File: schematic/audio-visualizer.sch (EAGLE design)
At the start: 18 parts, among them J3 455-1750-1-ND, U1 MSGEQ7P, U2 SN74AHCT125N

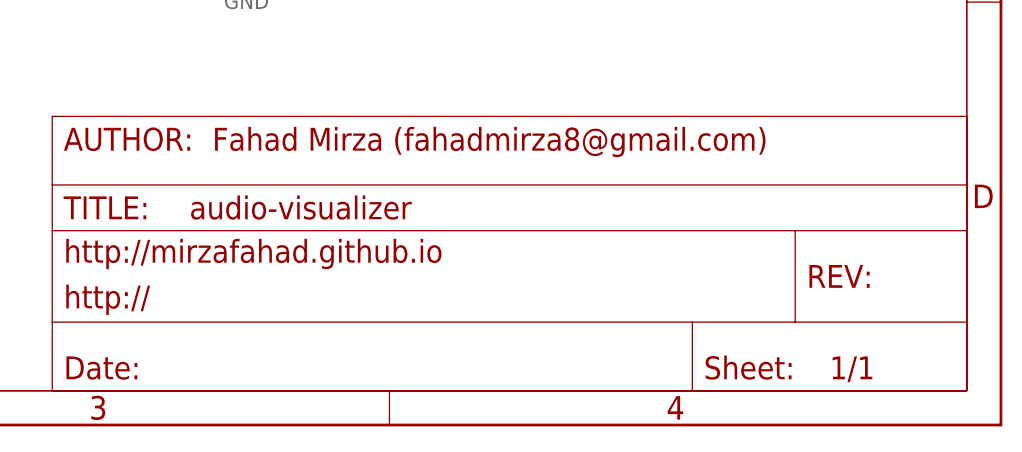
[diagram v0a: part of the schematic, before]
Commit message: pdf schematic added.
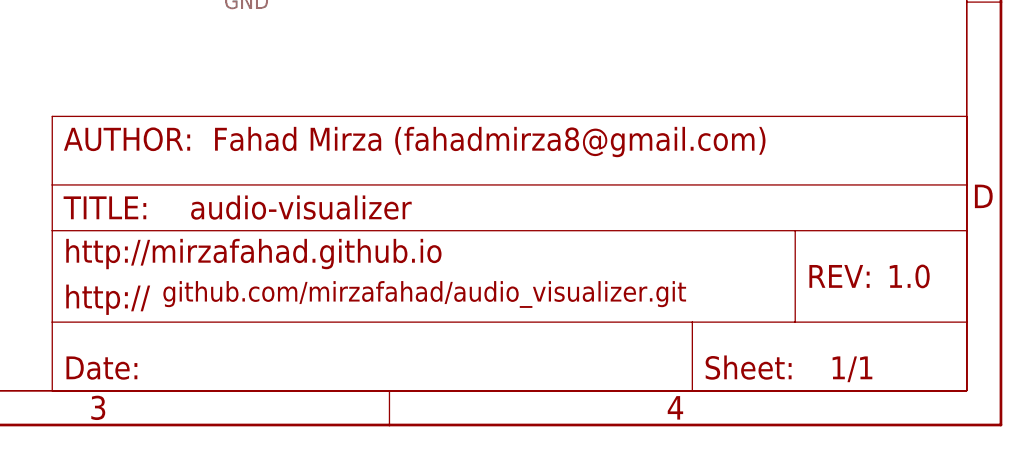
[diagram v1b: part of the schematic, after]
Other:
- note added: "1.0"
- note added: "github.com/mirzafahad/audio_visualizer.git"
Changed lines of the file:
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@@
 <layer number="94" name="Symbols" color="4" fill="1" visible="yes" active="yes"/>
 <layer number="95" name="Names" color="51" fill="1" visible="yes" active="yes"/>
-<layer number="96" name="Values" color="57" fill="1" visible="yes" active="yes"/>
+<layer number="96" name="Values" color="51" fill="1" visible="yes" active="yes"/>
 <layer number="97" name="Info" color="7" fill="1" visible="yes" active="yes"/>
 <layer number="98" name="Guide" color="6" fill="1" visible="yes" active="yes"/>
@@
 <wire x1="139.7" y1="96.52" x2="260.35" y2="96.52" width="0.1524" layer="94" style="shortdash"/>
 <wire x1="139.7" y1="77.216" x2="3.81" y2="77.216" width="0.1524" layer="94" style="shortdash"/>
+<text x="170.942" y="13.716" size="2.1844" layer="94" font="vector">github.com/mirzafahad/audio_visualizer.git</text>
+<text x="251.46" y="15.24" size="2.54" layer="94" font="vector">1.0</text>
 </plain>
 <instances>

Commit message: Updated folder structures.
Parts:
- removed C6: 1.0uF, SparkFun-Capacitors:1.0UF-0805-25V-(+80/-20%)
- removed PAGE1: FRAME_DINA4_L, dp_devices:FRAME_DINA4_L
- added J4, J5: 0022057035, SamacSys_Parts:0022057035
- added J6: PJ-002AH-SMT-TR, PersonalCollection:PJ-002AH-SMT-TR
- added J7: 22-05-7025, 22-05-7025:22-05-7025
- added LOGO1: OSHW-LOGOL-COPPER, SparkFun-Aesthetics:OSHW-LOGOL-COPPER
- added R5, R6, R8: 10K, SamacSys_Parts:R-US_R0805
- added S1: JS102011SAQN, JS102011SAQN:JS102011SAQN
- added U$2, U$3, U$4: FIDUCIAL, adafruit:FIDUCIAL
- C1: device SparkFun-Capacitors:1.0UF-0805-25V-(+80/-20%) -> SamacSys_Parts:CAP_0805
- C2: value 0.01uF -> 0.01uF/10V; device SparkFun-Capacitors:1.0UF-0805-25V-(+80/-20%) -> SamacSys_Parts:CAP_0805
- C3, C4: value 0.1uF -> 1uF/25V; device SparkFun-Capacitors:1.0UF-0805-25V-(+80/-20%) -> SamacSys_Parts:CAP_0805
- C5: value 1.0uF -> 1uF/25V; device SparkFun-Capacitors:1.0UF-0805-25V-(+80/-20%) -> SamacSys_Parts:CAP_0805
- C7: value 10TLV1000M10X10.5 -> 680uF/25V; device 10TLV1000M10X10.5:10TLV1000M10X10.5 -> SamacSys_Parts:EEE-FK1A681P
- J1, J2: value (none) -> SJ-3523-SMT-TR; device SparkFun-Connectors:AUDIO_JACK_2.5MM_HOLESONLY -> SamacSys_Parts:SJ-3523-SMT-TR
- J3: value 455-1750-1-ND -> 0022057035; device SparkFun-Connectors:CONN_03 -> SamacSys_Parts:0022057035
- MS1: value FEATHERWING_NODIM -> FEATHERWING_JUST_PINS; device adafruit:FEATHERWING_NODIM -> adafruit:FEATHERWING_JUST_PINS
- R1, R2: value 22K -> 10K; device SparkFun-Resistors:RESISTOR0805 -> SamacSys_Parts:R-US_R0805
- R3: device SparkFun-Resistors:RESISTOR0805 -> PersonalCollection:R-US_R0805
- R4: value 470 -> 330; device SparkFun-Resistors:RESISTOR0805 -> SamacSys_Parts:R-US_R0805
- U1: device SparkFun-IC-Special-Function:MSGEQ7DIL -> SamacSys_Parts:MSGEQ7DIL
- U2: device SN74AHCT125N:SN74AHCT125N -> SamacSys_Parts:SN74AHCT125N
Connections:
- removed net GPIO11: MS1.GPIO10, U1.STROBE
- removed net GPIO31: MS1.GPIO9, U1.RESET
- removed net GPIO7: MS1.GPIO11, U2.1A
- removed net GPIOA0: MS1.GPIOA0, U1.DCOUT
- new net DI_3.3: MS1.GPIO7, U2.1A
- new net LDR_ADC: J7.1, MS1.GPIOA5, R8.2
- new net MSG_DCOUT: MS1.GPIO30, U1.DCOUT
- new net MSG_RESET: MS1.GPIO11, U1.RESET
- new net MSG_STROBE: MS1.GPIO31, U1.STROBE
- new net N$10: J6.1, S1.3
- new net N$4: U2.1!OE
- new net N$7: J1.5, J2.5, R2.2
- new net N$9: J1.2, J2.2, R1.1
- new net PIR_OUT: J3.2, MS1.GPIO27
- net 3.3V: now also J7.2
- net 5V: now also J3.3, J4.3, J5.3, S1.1, S1.2; no longer C6.1, J3.1
- net DI: now also J4.2, R4.1; no longer J3.2, R4.2
- net GND: now also J1.1, J2.1, J3.1, J4.1, J5.1, J6.2, J6.3, R8.1; no longer C6.2, J1.SLEEVE, J2.SLEEVE, J3.3, U2.1!OE
- net N$1: now also R1.2, R5.2; no longer J1.RIGHT, J2.RIGHT, R1.1
- net N$2: now also R6.1; no longer J1.LEFT, J2.LEFT
- net N$3: now also R5.1, R6.2; no longer R1.2, R2.2
- net N$8: now also R4.2; no longer R4.1
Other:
- note added: "LDR"
- note added: "PIR Connector"
- note added: "Power Connector"
- note added: "github.com/mirzafahad/audio_visualizer"
- note removed: "NeoPixel"
- note removed: "github.com/mirzafahad/audio_visualizer.git"
- moved on the sheet: R1, R2, R3, R4, U1, U2
